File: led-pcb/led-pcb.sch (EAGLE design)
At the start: 9 parts

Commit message: updated pcbs
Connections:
- removed net DOUT: DOUT-12.1, DOUT-16.1, JP2.2
- new net DOUT-12: DOUT-12.1
- new net DOUT-16: DOUT-16.1
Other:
- moved on the sheet: JP2
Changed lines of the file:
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@@
 </plain>
 <instances>
-<instance part="JP2" gate="G$1" x="114.3" y="43.18"/>
+<instance part="JP2" gate="G$1" x="76.2" y="48.26"/>
 <instance part="VCC-16" gate="G$1" x="25.4" y="88.9"/>
 <instance part="GND-16" gate="G$1" x="25.4" y="73.66"/>
@@
 <segment>
 <pinref part="JP2" gate="G$1" pin="5"/>
-<wire x1="121.92" y1="48.26" x2="127" y2="48.26" width="0.1524" layer="91"/>
-<label x="121.92" y="48.26" size="1.778" layer="95"/>
+<wire x1="83.82" y1="53.34" x2="88.9" y2="53.34" width="0.1524" layer="91"/>
+<label x="83.82" y="53.34" size="1.778" layer="95"/>
 </segment>
 <segment>
@@
 <segment>
 <pinref part="JP2" gate="G$1" pin="4"/>
-<wire x1="121.92" y1="45.72" x2="127" y2="45.72" width="0.1524" layer="91"/>
-<label x="121.92" y="45.72" size="1.778" layer="95"/>
+<wire x1="83.82" y1="50.8" x2="88.9" y2="50.8" width="0.1524" layer="91"/>
+<label x="83.82" y="50.8" size="1.778" layer="95"/>
 </segment>
 <segment>
@@
 <segment>
 <pinref part="JP2" gate="G$1" pin="3"/>
-<wire x1="121.92" y1="43.18" x2="127" y2="43.18" width="0.1524" layer="91"/>
-<label x="121.92" y="43.18" size="1.778" layer="95"/>
+<wire x1="83.82" y1="48.26" x2="88.9" y2="48.26" width="0.1524" layer="91"/>
+<label x="83.82" y="48.26" size="1.778" layer="95"/>
 </segment>
 <segment>
@@
 </segment>
 </net>
-<net name="DOUT" class="0">
-<segment>
-<pinref part="JP2" gate="G$1" pin="2"/>
-<wire x1="121.92" y1="40.64" x2="127" y2="40.64" width="0.1524" layer="91"/>
-<label x="121.92" y="40.64" size="1.778" layer="95"/>
-</segment>
-<segment>
-<pinref part="DOUT-16" gate="G$1" pin="1"/>
-<wire x1="33.02" y1="43.18" x2="35.56" y2="43.18" width="0.1524" layer="91"/>
-<label x="33.02" y="43.18" size="1.778" layer="95"/>
-</segment>
+<net name="DOUT-12" class="0">
 <segment>
 <pinref part="DOUT-12" gate="G$1" pin="1"/>
@@
 </segment>
 </net>
+<net name="DOUT-16" class="0">
+<segment>
+<pinref part="DOUT-16" gate="G$1" pin="1"/>
+<wire x1="33.02" y1="43.18" x2="35.56" y2="43.18" width="0.1524" layer="91"/>
+<label x="33.02" y="43.18" size="1.778" layer="95"/>
+</segment>
+</net>

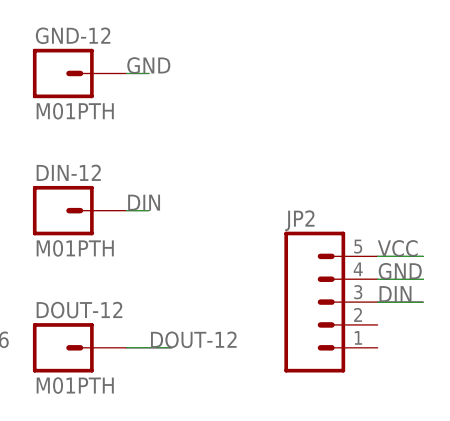
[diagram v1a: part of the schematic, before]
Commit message: adding bulb-2.brd and bulb-2.sch
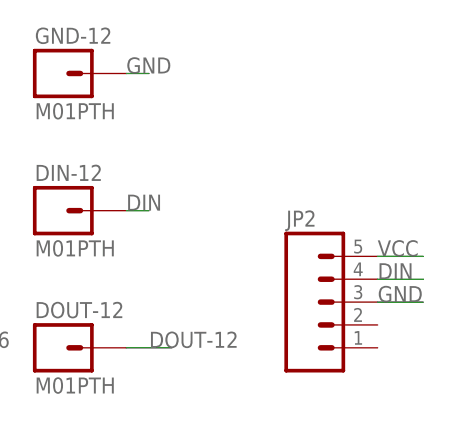
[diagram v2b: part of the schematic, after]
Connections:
- net DIN: now also JP2.4; no longer JP2.3
- net GND: now also JP2.3; no longer JP2.4
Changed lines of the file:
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@@
 <?xml version="1.0" encoding="utf-8"?>
 <!DOCTYPE eagle SYSTEM "eagle.dtd">
-<eagle version="6.5.0">
+<eagle version="7.2.0">
 <drawing>
 <settings>
@@
 <net name="VCC" class="0">
 <segment>
+<pinref part="VCC-16" gate="G$1" pin="1"/>
+<wire x1="33.02" y1="88.9" x2="35.56" y2="88.9" width="0.1524" layer="91"/>
+<label x="33.02" y="88.9" size="1.778" layer="95"/>
+</segment>
+<segment>
+<pinref part="VCC-12" gate="G$1" pin="1"/>
+<wire x1="55.88" y1="88.9" x2="60.96" y2="88.9" width="0.1524" layer="91"/>
+<label x="58.42" y="88.9" size="1.778" layer="95"/>
+</segment>
+<segment>
 <pinref part="JP2" gate="G$1" pin="5"/>
 <wire x1="83.82" y1="53.34" x2="88.9" y2="53.34" width="0.1524" layer="91"/>
 <label x="83.82" y="53.34" size="1.778" layer="95"/>
 </segment>
-<segment>
-<pinref part="VCC-16" gate="G$1" pin="1"/>
-<wire x1="33.02" y1="88.9" x2="35.56" y2="88.9" width="0.1524" layer="91"/>
-<label x="33.02" y="88.9" size="1.778" layer="95"/>
-</segment>
-<segment>
-<pinref part="VCC-12" gate="G$1" pin="1"/>
-<wire x1="55.88" y1="88.9" x2="60.96" y2="88.9" width="0.1524" layer="91"/>
-<label x="58.42" y="88.9" size="1.778" layer="95"/>
-</segment>
 </net>
 <net name="GND" class="0">
+<segment>
+<pinref part="GND-16" gate="G$1" pin="1"/>
+<wire x1="33.02" y1="73.66" x2="35.56" y2="73.66" width="0.1524" layer="91"/>
+<label x="33.02" y="73.66" size="1.778" layer="95"/>
+</segment>
+<segment>
+<pinref part="GND-12" gate="G$1" pin="1"/>
+<wire x1="55.88" y1="73.66" x2="58.42" y2="73.66" width="0.1524" layer="91"/>
+<label x="55.88" y="73.66" size="1.778" layer="95"/>
+</segment>
+<segment>
+<pinref part="JP2" gate="G$1" pin="3"/>
+<wire x1="83.82" y1="48.26" x2="88.9" y2="48.26" width="0.1524" layer="91"/>
+<label x="83.82" y="48.26" size="1.778" layer="95"/>
+</segment>
+</net>
+<net name="DIN" class="0">
+<segment>
+<pinref part="DIN-16" gate="G$1" pin="1"/>
+<wire x1="33.02" y1="58.42" x2="35.56" y2="58.42" width="0.1524" layer="91"/>
+<label x="33.02" y="58.42" size="1.778" layer="95"/>
+</segment>
+<segment>
+<pinref part="DIN-12" gate="G$1" pin="1"/>
+<wire x1="55.88" y1="58.42" x2="58.42" y2="58.42" width="0.1524" layer="91"/>
+<label x="55.88" y="58.42" size="1.778" layer="95"/>
+</segment>
 <segment>
 <pinref part="JP2" gate="G$1" pin="4"/>
@@
 <label x="83.82" y="50.8" size="1.778" layer="95"/>
 </segment>
-<segment>
-<pinref part="GND-16" gate="G$1" pin="1"/>
-<wire x1="33.02" y1="73.66" x2="35.56" y2="73.66" width="0.1524" layer="91"/>
-<label x="33.02" y="73.66" size="1.778" layer="95"/>
-</segment>
-<segment>
-<pinref part="GND-12" gate="G$1" pin="1"/>
-<wire x1="55.88" y1="73.66" x2="58.42" y2="73.66" width="0.1524" layer="91"/>
-<label x="55.88" y="73.66" size="1.778" layer="95"/>
-</segment>
 </net>
-<net name="DIN" class="0">
-<segment>
-<pinref part="JP2" gate="G$1" pin="3"/>
-<wire x1="83.82" y1="48.26" x2="88.9" y2="48.26" width="0.1524" layer="91"/>
-<label x="83.82" y="48.26" size="1.778" layer="95"/>
-</segment>
-<segment>
-<pinref part="DIN-16" gate="G$1" pin="1"/>
-<wire x1="33.02" y1="58.42" x2="35.56" y2="58.42" width="0.1524" layer="91"/>
-<label x="33.02" y="58.42" size="1.778" layer="95"/>
-</segment>
-<segment>
-<pinref part="DIN-12" gate="G$1" pin="1"/>
-<wire x1="55.88" y1="58.42" x2="58.42" y2="58.42" width="0.1524" layer="91"/>
-<label x="55.88" y="58.42" size="1.778" layer="95"/>
-</segment>
-</net>
